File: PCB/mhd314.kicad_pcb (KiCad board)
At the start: 4 copper layers, 65 x 56 mm, 188 parts, among them J1 Raspberry_Pi_2_3, J2 AudioJack_Pentaconn, J4 AudioJack3_SwitchTR, Q1 AO3401A, SW1 SW_Push, U1 ES9038Q2M, U10 AT24CS64-SSHM, U11 OPA1622, U13 OPA1622, U2 OPA1612AxD, U3 OPA1612AxD, U4 OPA1622, U5 LM317_SOT-223, U6 LM317_SOT-223, U7 TPS65131RGE, U8 LM317_SOT-223, U9 LM337_SOT223, Y1 ASE-50MHz

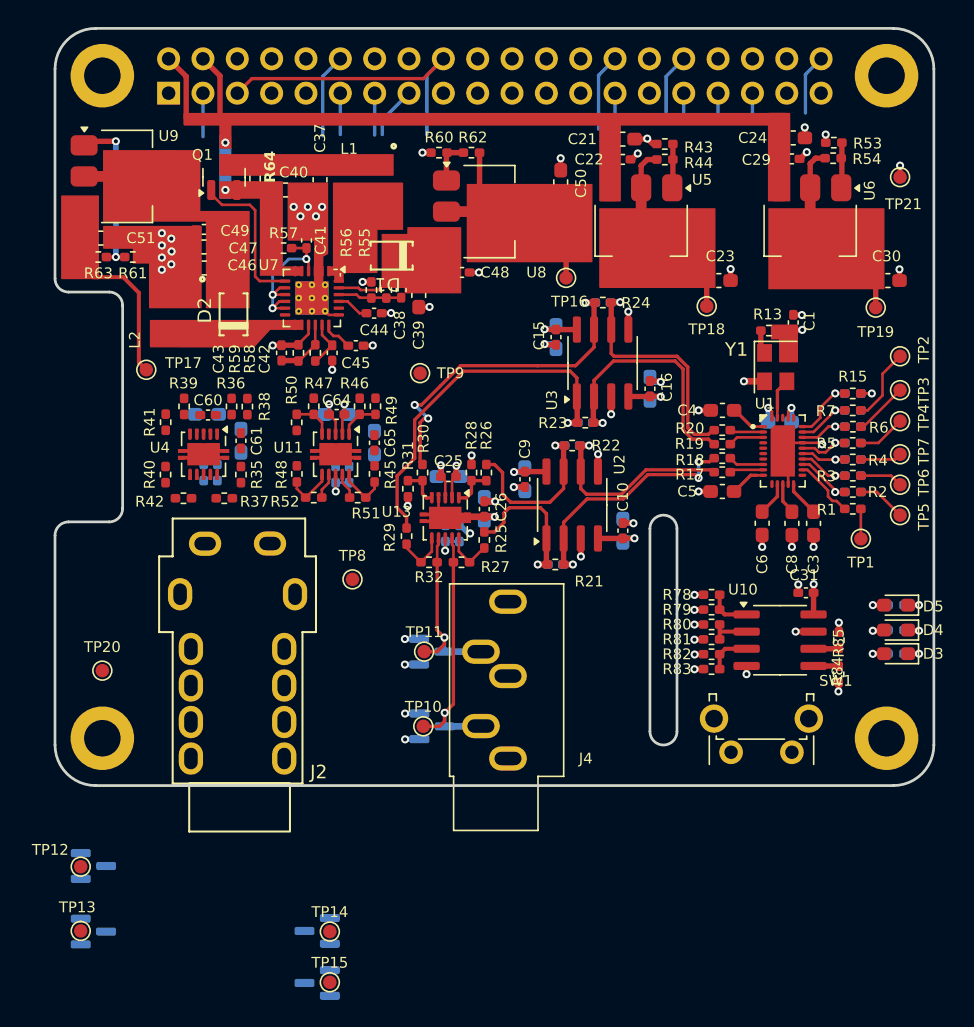
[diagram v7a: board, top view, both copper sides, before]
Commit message: Advances all basic track routing. Pending power planes, grounding and optimization
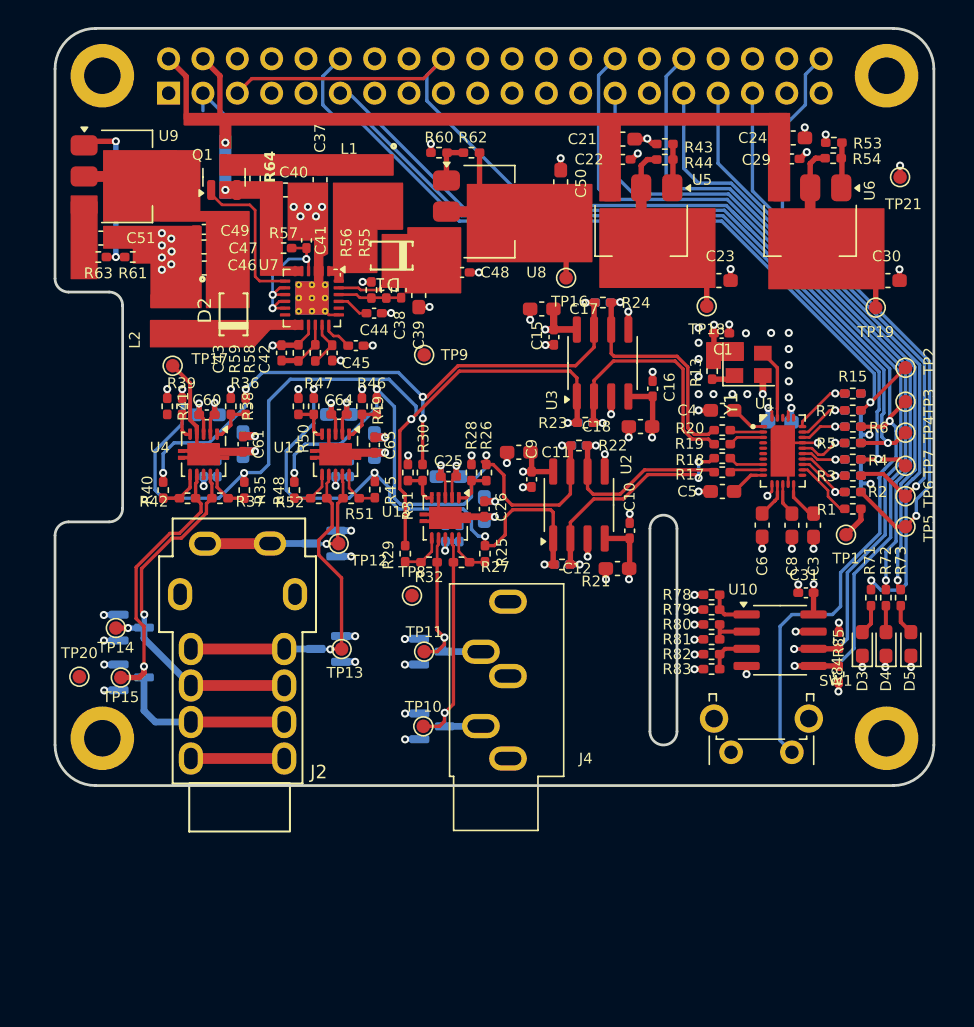
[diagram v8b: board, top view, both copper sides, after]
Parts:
- C11, C12, C17, C18, R71, R72, R73: moved to F.Cu
- D1, D2: footprint _mahaudio KiCad Library:SOD-123_425-04_ONS -> mahaudio_footprints:SOD-123_425-04_ONS
- moved TP12 30.6 mm to (87.5, 94.4), turned to 180 degrees
- moved D8 29.3 mm to (86.4, 94.3), turned to 180 degrees
- moved TP13 28.4 mm to (87.7, 102.2), turned to 180 degrees
- moved TP14 27.5 mm to (71.0, 100.6), turned to 180 degrees
- moved TP15 27.3 mm to (71.4, 104.3), turned to 180 degrees
- moved D9 27.2 mm to (86.7, 102.1), turned to 180 degrees
- moved D11 26.5 mm to (72.1, 104.2), turned to 0 degrees
- moved D10 26.3 mm to (72.1, 100.6), turned to 0 degrees
- moved C1 5.36 mm to (115.8, 78.8), turned to 0 degrees
- moved R13 5.16 mm to (115.1, 81.6), turned to 90 degrees
- moved TP8 4.56 mm to (92.9, 98.2)
- moved R71 4.54 mm to (126.8, 98.4), turned to 90 degrees
- moved D5 3.07 mm to (129.8, 101.8), turned to 90 degrees
- moved C18 2.89 mm to (109.8, 85.7), turned to 0 degrees
- moved C12 2.83 mm to (108.1, 96.2), turned to 0 degrees
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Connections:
- C1 pad 1: +3.3V -> +3.3VA
- R13 pad 2: +3.3V -> +3.3VA
- Y1 pad 4: +3.3V -> +3.3VA
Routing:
- net /BRD_ONOFF: track 26.4 -> 103.6 mm, vias 0 -> 1
- net /BRD_ID_SD: track 4.33 -> 63.8 mm, vias 0 -> 1
- net /BRD_ID_SC: track 7.56 -> 66.9 mm, vias 0 -> 1
- net /DAC_SDA: track 8.72 -> 66.4 mm, vias 0 -> 1
- net /DAC_PCM_CLK: track 9.30 -> 63.3 mm, vias 0 -> 1
- net /DAC_RESETB: track 6.63 -> 58.0 mm, vias 0 -> 1
- net /BRD_LED0: track 5.24 -> 50.3 mm, vias 0 -> 1
- net /BRD_LED1: track 2.18 -> 46.7 mm, vias 0 -> 1
- net /BRD_LED2: track 2.16 -> 45.8 mm, vias 0 -> 1
- net /AMP/BalDiffAmp_R/BALDIFFAMP_IN_P: track 27.3 -> 66.1 mm, vias 1 -> 4
- net /DAC_PCM_DATA: track 8.09 -> 45.4 mm, vias 0 -> 1
- net /DAC_PCM_FS: track 5.24 -> 39.9 mm, vias 0 -> 1
- net /OUT_BAL_R_N: track 0.00 -> 33.4 mm, vias 0 -> 1
- net /AMP/BalDiffAmp_L/BALDIFFAMP_IN_N: track 12.8 -> 44.6 mm, vias 1 -> 4
- net /AMP/BalDiffAmp_L/BALDIFFAMP_IN_P: track 11.1 -> 41.5 mm, vias 1 -> 4
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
